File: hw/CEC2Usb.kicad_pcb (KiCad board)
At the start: 2 copper layers, 23.7 x 30.5 mm, 33 parts, among them J1 USB_B_Mini, J2 HDMI_A, J3 HDMI_A, J4 ICSP, Q1 BC817, U1 TLV70233_SOT23-5, U2 ATmega32U2-AU, Y1 16MHz

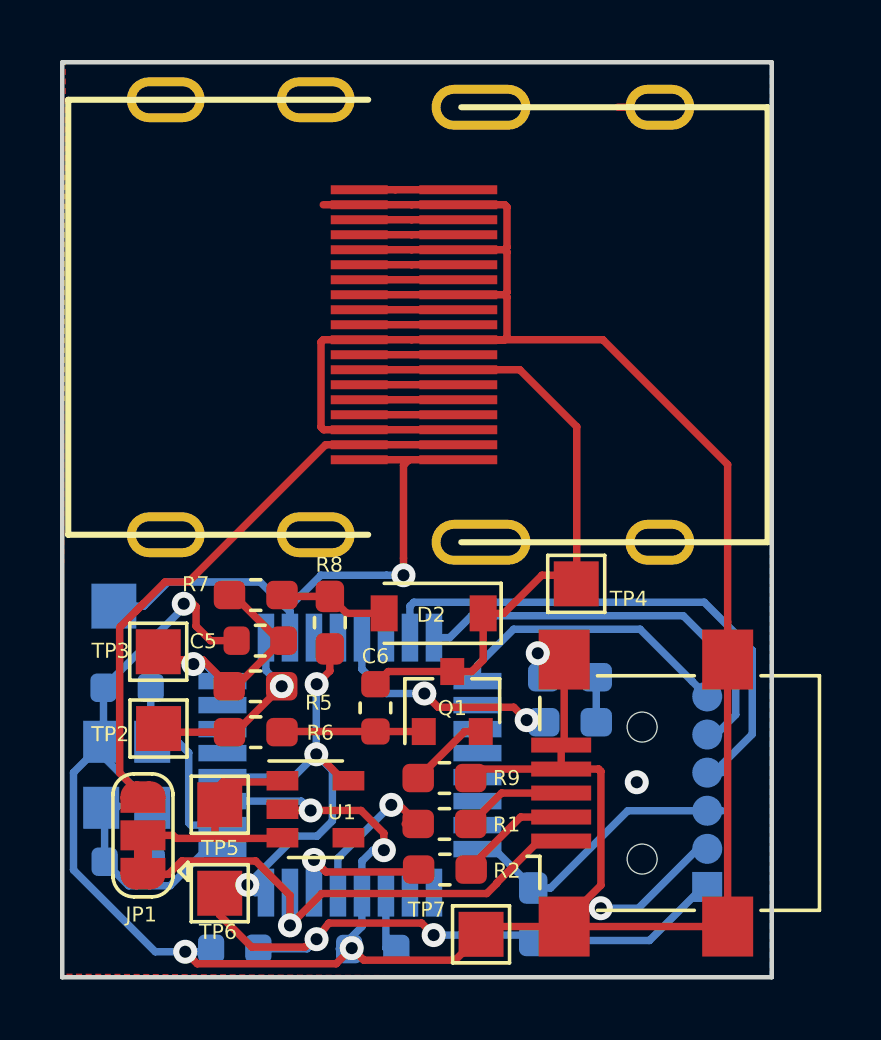
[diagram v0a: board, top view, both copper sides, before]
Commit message: [Hw] v0.2, Fixed mistakes, moved stuff, add LEDs conn
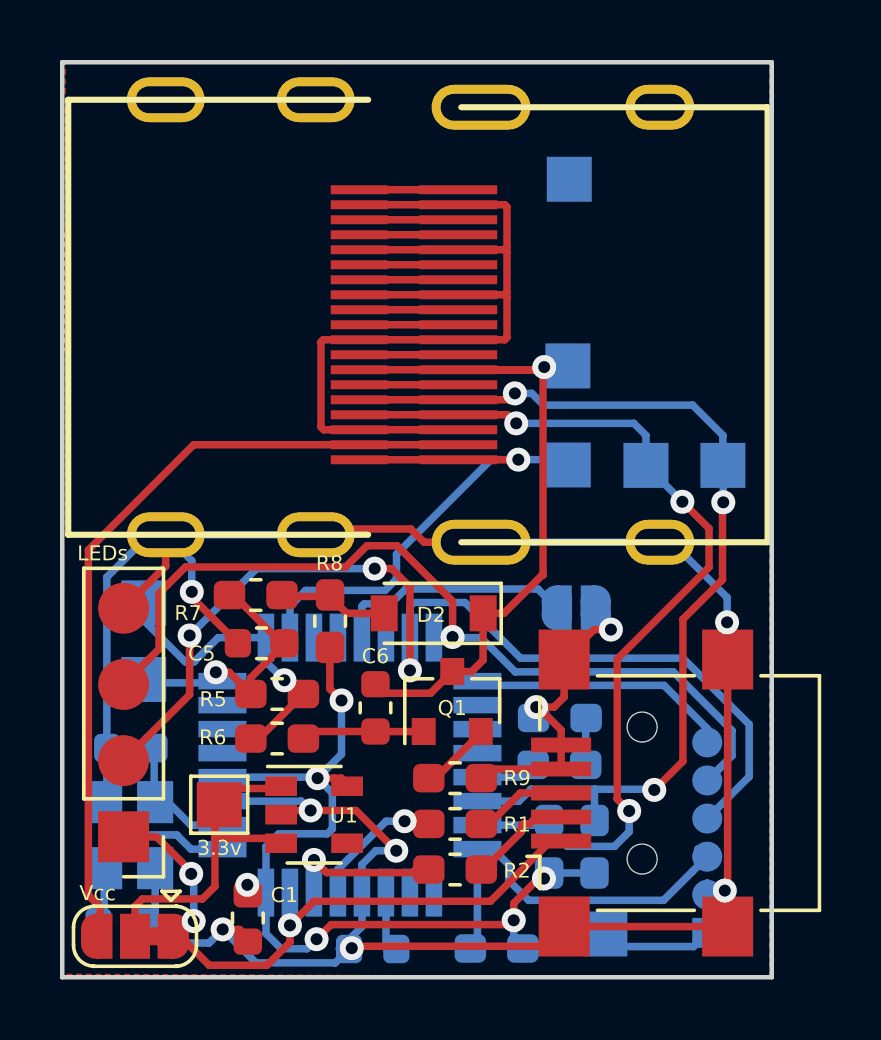
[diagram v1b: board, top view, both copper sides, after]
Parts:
- added JP2: DFU, Jumper:SolderJumper-2_P1.3mm_Open_RoundedPad1.0x1.5mm, B.Cu at (82.2, 62.7)
- added LEDs: LEDs, Connector_PinHeader_2.54mm:PinHeader_1x04_P2.54mm_Vertical, F.Cu at (67.1, 70.3)
- added R11: 4.7k, Resistor_SMD:R_0603_1608Metric_Pad1.05x0.95mm_HandSolder, B.Cu at (81.3, 70.7)
- added R12: 4.7k, Resistor_SMD:R_0603_1608Metric_Pad1.05x0.95mm_HandSolder, B.Cu at (82.8, 70.7)
- added TP8: SDA, TestPoint:TestPoint_Pad_1.5x1.5mm, B.Cu at (84.6, 57.9)
- added TP9: SCL, TestPoint:TestPoint_Pad_1.5x1.5mm, B.Cu at (87.1, 57.9)
- 3.3v: renamed from TP5; value TestPoint -> Vcc
- C1: moved to F.Cu
- D1: value LED_Small -> LED
- TP1: value TestPoint_Alt -> HPD
- TP2: value TestPoint_Alt -> CEC_OUT; moved to B.Cu
- TP3: value TestPoint_Alt -> CEC_IN; moved to B.Cu
- TP4: value TestPoint_Alt -> CEC; moved to B.Cu
- TP6: value TestPoint -> 3.3v; moved to B.Cu
- TP7: value TestPoint -> GND; moved to B.Cu
- moved TP7 25.3 mm to (82.0, 48.4)
- moved TP1 15.9 mm to (82.0, 57.9)
- moved TP6 12.9 mm to (83.2, 73.6)
- moved TP4 7.27 mm to (82.0, 54.6)
- moved TP2 4.22 mm to (67.8, 62.5)
- moved Vcc 3.37 mm to (67.5, 73.6), turned to 180 degrees
- moved C2 2.04 mm to (67.1, 73.2)
- moved Y1 2.02 mm to (67.3, 70.3)
- moved C3 2.01 mm to (67.4, 67.4)
- moved R3 1.67 mm to (79.6, 74.0), turned to 180 degrees
- moved J4 1.53 mm to (86.6, 73.5)
- moved R4 1.46 mm to (81.7, 67.9)
- moved D1 1.40 mm to (81.7, 66.4)
- moved C1 1.11 mm to (71.3, 73.0), turned to 270 degrees
- moved TP3 1.04 mm to (67.8, 65.1)
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- renumbered JP1 to Vcc
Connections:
- net Net-(J4-Pad4) renamed /SPI_CLK
- net Net-(J4-Pad5) renamed /SPI_MOSI
- R4 pad 2: Net-(R4-Pad2) -> /LED
- U2 pad 13: Net-(R4-Pad2) -> Net-(JP2-Pad1)
- U2 pad 21: Net-(U2-Pad21) -> /LED
- U2 pad 22: Net-(U2-Pad22) -> /SCL
- U2 pad 23: Net-(U2-Pad23) -> /SDA
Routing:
- net /SCL: track 3.30 -> 32.7 mm, vias 0 -> 3
- net /SDA: track 3.30 -> 30.9 mm, vias 0 -> 3
- net /SPI_CLK: track 17.7 -> 35.3 mm, vias 0 -> 3
- net /SPI_MOSI: track 14.0 -> 30.5 mm, vias 0 -> 1
- net Net-(JP2-Pad1): track 0.00 -> 8.04 mm
- net Net-(R4-Pad2): track 7.84 -> 0.00 mm, vias 2 -> 0
- net +5V: track 20.1 -> 26.7 mm
- net GND: track 139.5 -> 133.6 mm, vias 8 -> 9
- net VCC: track 18.0 -> 22.5 mm, vias 1 -> 3
- net Net-(J4-Pad3): track 9.76 -> 13.6 mm
- net /CEC_OUT: track 6.63 -> 10.3 mm
- net Net-(C3-Pad1): track 6.68 -> 3.84 mm
- net /CEC: track 22.1 -> 24.8 mm, vias 0 -> 1
- net /LED: track 0.00 -> 2.03 mm
- net Net-(JP1-Pad2): track 9.65 -> 11.7 mm
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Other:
- board text added: "RedoX 10/2k19 www.redox.ws"
- board text added: "v0.2"
- board text removed: "RedoX 09/2k19 www.redox.ws"
